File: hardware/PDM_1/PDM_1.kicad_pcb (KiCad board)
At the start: 4 copper layers, 55 x 100 mm, 148 parts, among them IC2 BTS722204ESAXUMA1, IC3 BTS722204ESAXUMA1, IC4 BTS722204ESAXUMA1, IC5 BTS722204ESAXUMA1, J1 FTSH-107-01-L-DV-K-A, J2 UPT-08-01-01-L-RA, J5 UPT-02-01-01-X-RA, J6 Conn_01x06, J7 UPT-08-01-01-L-RA, U1 STM32G0C1KCTxN, U2 LD1117S33TR_SOT223, U3 LM2675M-5.0/NOPB, U5 MCP2542FDxMF

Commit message: Koniec
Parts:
- D3: value PESD24VF1BLYL -> SMAJ24CA-13-F; footprint PESD24VF1BLYL:PESD5V0S1BL315 -> Diode_SMD:D_SMA
- moved D3 1.28 mm to (162.3, 75.7)
- moved Dr1 0.92 mm to (162.3, 68.5)
- moved F1 0.80 mm to (167.4, 69.5)
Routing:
- net GND: vias 223 -> 220

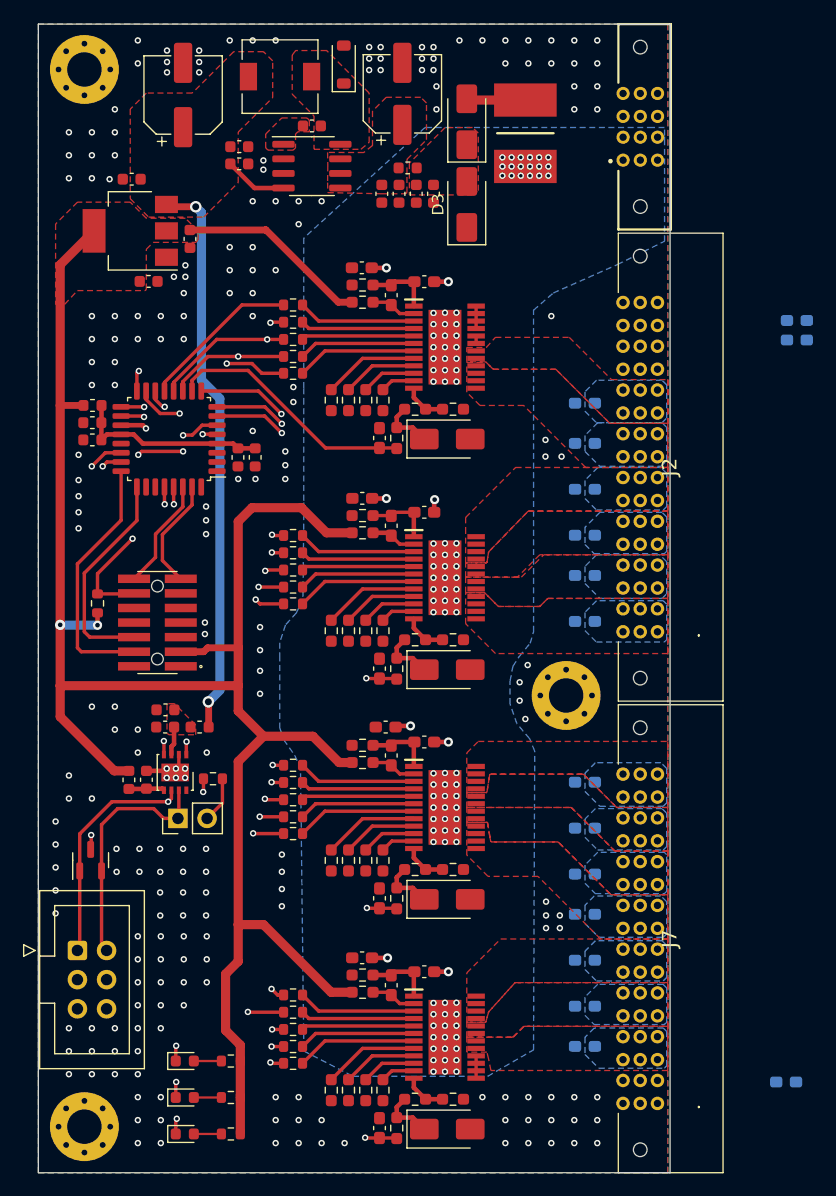
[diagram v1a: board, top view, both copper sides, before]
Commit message: Transfer from PDM to simple FuseBox
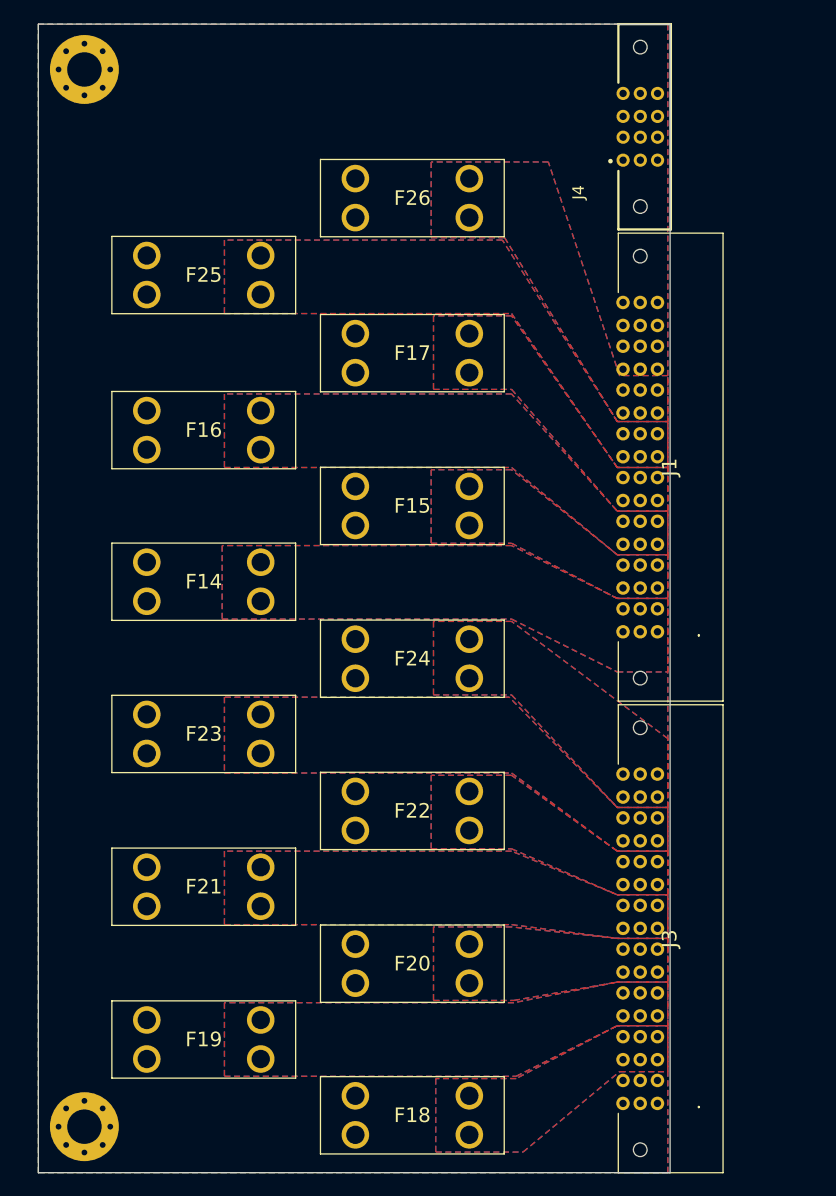
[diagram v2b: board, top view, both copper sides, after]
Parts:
- removed C1, C3: 100n, Inductor_SMD:L_0603_1608Metric
- removed C10, C13, C16, C17, C19, C7, C8: 100n, Capacitor_SMD:C_0603_1608Metric
- removed C11, C15, C5: 1u, Capacitor_SMD:C_0603_1608Metric
- removed C12: 10n, Capacitor_SMD:C_0603_1608Metric
- removed C14: 68u, Capacitor_SMD:CP_Elec_6.3x5.4
- removed C18: 10uF, Capacitor_SMD:C_0603_1608Metric
- removed C2, C4: 4.7u, Inductor_SMD:L_0603_1608Metric
- removed C29, C37, C45, C53: 220p, Capacitor_SMD:C_0603_1608Metric_Pad1.08x0.95mm_HandSolder
- removed C30, C38, C46, C54: 100n, Capacitor_SMD:C_0603_1608Metric_Pad1.08x0.95mm_HandSolder
- removed C31, C39, C47, C55: 22n, Capacitor_SMD:C_0603_1608Metric_Pad1.08x0.95mm_HandSolder
- removed C32, C40, C48, C56: 470n, Capacitor_SMD:C_0603_1608Metric_Pad1.08x0.95mm_HandSolder
- removed C33, C34, C35, C36, C41, C42, C43, C44, C49, C50, C51, C52, C57, C58, C59, C60: 10n, Capacitor_SMD:C_0603_1608Metric_Pad1.08x0.95mm_HandSolder
- removed C6: 10u, Capacitor_SMD:C_0603_1608Metric
- removed C9: 100u, Capacitor_SMD:CP_Elec_6.3x7.7
- removed D1, D2, D7: LED, LED_SMD:LED_0603_1608Metric
- removed D10, D11, D8, D9: D_Schottky, Diode_SMD:D_SMA
- removed D3: SMAJ24CA-13-F, Diode_SMD:D_SMA
- removed D4: D_Schottky_Small, Diode_SMD:D_SOD-123
- removed D5: PESD2CAN.215, Package_TO_SOT_SMD:SOT-23
- removed Dr1: SS34ALH, Diode_SMD:D_SMA
- removed F1: 2920L050_72DR, 2920l:FUSC7451X125N
- removed FB1: FerriteBead_Small, Inductor_SMD:L_0603_1608Metric
- removed FB2, FB3: 60R@100MHz, Inductor_SMD:L_0603_1608Metric
- removed G***: LOGO, logos:PUTM_LOGO_15mm
- removed G***: LOGO, Logos:SignatureBox25mm
- removed IC2, IC3, IC4, IC5: BTS722204ESAXUMA1, Samacsys:SOP65P600X115-25N
- removed J2, J7: UPT-08-01-01-L-RA, proper_8pin:UPT080101LRA
- removed J5: UPT-02-01-01-X-RA, 2pin:SAMTEC_UPT-02-01-01-X-RA
- removed J6: Conn_01x06, Connector_IDC:IDC-Header_2x03_P2.54mm_Vertical
- removed JP1: Jumper_2_Bridged, Connector_PinHeader_2.54mm:PinHeader_1x02_P2.54mm_Vertical
- removed L1: 300n, Inductor_SMD:L_0603_1608Metric
- removed L4: 47u, Inductor_SMD:L_6.3x6.3_H3
- removed R1: 120, Resistor_SMD:R_0603_1608Metric
- removed R10, R2, R3, R4, R47, R48, R49, R5, R50, R51, R52, R53, R6, R7, R8, R9: 1.2k, Resistor_SMD:R_0603_1608Metric
- removed R11, R13, R20, R22, R29, R31, R38, R40: 4.7k, Resistor_SMD:R_0603_1608Metric_Pad0.98x0.95mm_HandSolder
- removed R12, R21, R30, R39: 470, Resistor_SMD:R_0603_1608Metric_Pad0.98x0.95mm_HandSolder
- removed R14, R15, R16, R17, R23, R24, R25, R26, R32, R33, R34, R35, R41, R42, R43, R44: 10k, Resistor_SMD:R_0603_1608Metric_Pad0.98x0.95mm_HandSolder
- removed R18, R27, R36, R45: 47, Resistor_SMD:R_0603_1608Metric_Pad0.98x0.95mm_HandSolder
- removed R19, R28, R37, R46: 1.2k, Resistor_SMD:R_0603_1608Metric_Pad0.98x0.95mm_HandSolder
- removed R54: 100k, Resistor_SMD:R_0603_1608Metric
- removed R55, R56, R57: 330, Resistor_SMD:R_0603_1608Metric
- removed R58, R59, R60, R61: 4.7k, Resistor_SMD:R_0603_1608Metric
- removed the REF** at (170.9, 118.5)
- removed U1: STM32G0C1KCTxN, Package_QFP:LQFP-32_7x7mm_P0.8mm
- removed U2: LD1117S33TR_SOT223, Package_TO_SOT_SMD:SOT-223-3_TabPin2
- removed U3: LM2675M-5.0/NOPB, Package_SO:SOIC-8_3.9x4.9mm_P1.27mm
- removed U5: MCP2542FDxMF, Package_DFN_QFN:DFN-8-1EP_3x3mm_P0.65mm_EP1.55x2.4mm
- added F14: Fuse, LIB_3568:3568, F.Cu at (134.4, 110.2)
- added F15: Fuse, LIB_3568:3568, F.Cu at (152.6, 103.6)
- added F16: Fuse, LIB_3568:3568, F.Cu at (134.4, 97.0)
- added F17: Fuse, LIB_3568:3568, F.Cu at (152.6, 90.3)
- added F18: Fuse, LIB_3568:3568, F.Cu at (152.6, 156.7)
- added F19: Fuse, LIB_3568:3568, F.Cu at (134.4, 150.1)
- added F20: Fuse, LIB_3568:3568, F.Cu at (152.6, 143.5)
- added F21: Fuse, LIB_3568:3568, F.Cu at (144.4, 133.4)
- added F22: Fuse, LIB_3568:3568, F.Cu at (162.5, 126.8)
- added F23: Fuse, LIB_3568:3568, F.Cu at (144.4, 120.1)
- added F24: Fuse, LIB_3568:3568, F.Cu at (162.5, 113.5)
- added F25: Fuse, LIB_3568:3568, F.Cu at (144.4, 80.1)
- added F26: Fuse, LIB_3568:3568, F.Cu at (162.5, 73.4)
- added J3: UPT-08-01-01-L-RA, proper_8pin:UPT080101LRA, F.Cu at (178.9, 154.0)
- added J4: UPT-02-01-01-X-RA, 2pin:SAMTEC_UPT-02-01-01-X-RA, F.Cu at (177.4, 68.9)
- J1: value FTSH-107-01-L-DV-K-A -> UPT-08-01-01-L-RA; footprint FTSH-107-01-L-DV-K-A:FTSH-107-XX-YYY-DV-K-A -> proper_8pin:UPT080101LRA
- moved J1 43.5 mm to (178.9, 112.9)
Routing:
- net +3.3V: track 183.7 -> 0.00 mm, vias 2 -> 0
- net /SPI1_NSS: track 78.2 -> 0.00 mm, vias 4 -> 0
- net /SPI1_SCK: track 77.3 -> 0.00 mm, vias 4 -> 0
- net /FUSE1_IS: track 73.3 -> 0.00 mm, vias 2 -> 0
- net /LED3: track 71.1 -> 0.00 mm, vias 2 -> 0
- net /LED2: track 66.6 -> 0.00 mm, vias 2 -> 0
- net /LED1: track 62.1 -> 0.00 mm, vias 2 -> 0
- net /SPI1_MOSI: track 61.1 -> 0.00 mm, vias 2 -> 0
- net /LHI_1: track 55.2 -> 0.00 mm, vias 2 -> 0
- net +5V: track 54.7 -> 0.00 mm, vias 2 -> 0
- net /FUSE2_IS: track 54.1 -> 0.00 mm, vias 2 -> 0
- net /FUSE3_IS: track 36.5 -> 0.00 mm, vias 2 -> 0
- net /LHI_2: track 35.7 -> 0.00 mm, vias 2 -> 0
- net /CAN_RXD: track 30.5 -> 0.00 mm, vias 2 -> 0
- net /CAN_TXD: track 30.1 -> 0.00 mm, vias 2 -> 0
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- added copper zone on In2.Cu, net +BATT
- added copper zone on B.Cu, net /AIR / IR / DIAGPORT
- added copper zone on F.Cu, net /AIR / IR / DIAGPORT
- added copper zone on In1.Cu, net /AIR / IR / DIAGPORT
- added copper zone on In2.Cu, net /AIR / IR / DIAGPORT
- added copper zone on B.Cu, net /BRAKE / DASH / FRONT BOX
- added copper zone on F.Cu, net /BRAKE / DASH / FRONT BOX
- added copper zone on In1.Cu, net /BRAKE / DASH / FRONT BOX
- added copper zone on In2.Cu, net /BRAKE / DASH / FRONT BOX
- added copper zone on B.Cu, net /FAN
- added copper zone on F.Cu, net /FAN
- added copper zone on In1.Cu, net /FAN
- added copper zone on In2.Cu, net /FAN
- added copper zone on B.Cu, net /HV LOGIKA
- added copper zone on F.Cu, net /HV LOGIKA
- added copper zone on In1.Cu, net /HV LOGIKA
- added copper zone on In2.Cu, net /HV LOGIKA
- added copper zone on B.Cu, net /INVERTER
- added copper zone on F.Cu, net /INVERTER
- added copper zone on In1.Cu, net /INVERTER
- added copper zone on In2.Cu, net /INVERTER
- added copper zone on B.Cu, net /PC 1/2
- added copper zone on F.Cu, net /PC 1/2
- added copper zone on In1.Cu, net /PC 1/2
- added copper zone on In2.Cu, net /PC 1/2
- added copper zone on B.Cu, net /PC 3 / 4
- added copper zone on F.Cu, net /PC 3 / 4
- added copper zone on In1.Cu, net /PC 3 / 4
- added copper zone on In2.Cu, net /PC 3 / 4
- added copper zone on B.Cu, net /PC 5
- added copper zone on F.Cu, net /PC 5
- added copper zone on In1.Cu, net /PC 5
- added copper zone on In2.Cu, net /PC 5
- added copper zone on B.Cu, net /PUMP 1
- added copper zone on F.Cu, net /PUMP 1
- added copper zone on In1.Cu, net /PUMP 1
- added copper zone on In2.Cu, net /PUMP 1
- added copper zone on B.Cu, net /PUMP 2
- added copper zone on F.Cu, net /PUMP 2
- added copper zone on In1.Cu, net /PUMP 2
- added copper zone on In2.Cu, net /PUMP 2
- added copper zone on B.Cu, net /REARBOX 5
- added copper zone on F.Cu, net /REARBOX 5
- added copper zone on In1.Cu, net /REARBOX 5
- added copper zone on In2.Cu, net /REARBOX 5
- added copper zone on B.Cu, net /SDC / ASMS
- added copper zone on F.Cu, net /SDC / ASMS
- added copper zone on In1.Cu, net /SDC / ASMS
- added copper zone on In2.Cu, net /SDC / ASMS
- added copper zone on B.Cu, net /TSAL / BSPD
- added copper zone on F.Cu, net /TSAL / BSPD
- added copper zone on In1.Cu, net /TSAL / BSPD
- added copper zone on In2.Cu, net /TSAL / BSPD
- removed copper zone on F.Cu, net +3.3V
- removed copper zone on F.Cu, net +5V
- removed copper zone on F.Cu, net /CAN/CAN_VDD
- removed copper zone on F.Cu, net /power/CB
- removed copper zone on F.Cu, net /power/SW_L
- removed copper zone on F.Cu, net /power/VIN_L
- removed copper zone on F.Cu, net /power/VIN_SW_REG
- removed copper zone on B.Cu, net GND
- removed copper zone on In2.Cu, net GND
- removed copper zone on B.Cu, net OUT1_0
- removed copper zone on F.Cu, net OUT1_0
- removed copper zone on B.Cu, net OUT1_1
- removed copper zone on F.Cu, net OUT1_1
- removed copper zone on B.Cu, net OUT1_2
- removed copper zone on F.Cu, net OUT1_2
- removed copper zone on B.Cu, net OUT2_0
- removed copper zone on F.Cu, net OUT2_0
- removed copper zone on B.Cu, net OUT2_1
- removed copper zone on F.Cu, net OUT2_1
- removed copper zone on B.Cu, net OUT2_2
- removed copper zone on F.Cu, net OUT2_2
- removed copper zone on B.Cu, net OUT2_3
- removed copper zone on F.Cu, net OUT2_3
- removed copper zone on B.Cu, net OUT3_0
- removed copper zone on F.Cu, net OUT3_0
- removed copper zone on B.Cu, net OUT3_1
- removed copper zone on F.Cu, net OUT3_1
- removed copper zone on B.Cu, net OUT3_2
- removed copper zone on F.Cu, net OUT3_2
- removed copper zone on B.Cu, net OUT3_3
- removed copper zone on F.Cu, net OUT3_3
- removed copper zone on B.Cu, net OUT4_2
- removed copper zone on F.Cu, net OUT4_2
- removed copper zone on B.Cu, net OUT4_3
- removed copper zone on F.Cu, net OUT4_3

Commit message: Logo and description added
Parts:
- added G***: LOGO, logos:PUTM_LOGO_13mm, F.Cu at (161.0, 65.0)
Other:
- board text added: "FUSE BOX v1.0"
- board text removed: "Kacper Biadała"
- board text removed: "v${REVISION}"
